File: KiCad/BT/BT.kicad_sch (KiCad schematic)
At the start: 54 parts, among them J1 UJC-HP-3-SMT-TR, J2 2328702-8, J3 Conn_01x05, SW1 PTS840ESDPMSMTRLFS, U1 LDK130PU-R, U2 STBC08PMR, U3 STM6601CQ2BDM6F, U4 BMD-350-A-R, U5 SSM6L61NU, U6 SSM6L61NU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

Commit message: swapped SWDIO/SWCLK, BM pin moved to AN4
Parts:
- R14: value 4M -> 100K
- R15: value 3M -> 75K
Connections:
- net BM: now also U4.45 (P0.28/AIN4); no longer U4.13 (P0.12)
- net BM_EN: now also U4.32 (P0.27); no longer U4.45 (P0.28/AIN4)
- net LED_EN: now also U4.34 (P0.26); no longer U4.32 (P0.27)
- net SWDCLK: now also J3.4 (Pin_4), U4.4 (SWCLK); no longer J3.3 (Pin_3), U4.5 (SWDIO)
- net SWDIO: now also J3.3 (Pin_3), U4.5 (SWDIO); no longer J3.4 (Pin_4), U4.4 (SWCLK)
- net XSHUT1: now also U4.19 (P0.06); no longer U4.12 (P0.13)
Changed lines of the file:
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@@
   (no_connect (at 231.14 64.77))
   (no_connect (at 180.34 49.53))
-  (no_connect (at 231.14 57.15))
+  (no_connect (at 231.14 44.45))
   (no_connect (at 92.71 48.26))
-  (no_connect (at 231.14 74.93))
+  (no_connect (at 180.34 77.47))
   (no_connect (at 250.19 162.56))
   (no_connect (at 231.14 80.01))
   (no_connect (at 64.77 90.17))
   (no_connect (at 180.34 69.85))
-  (no_connect (at 231.14 44.45))
+  (no_connect (at 180.34 74.93))
   (no_connect (at 231.14 46.99))
   (no_connect (at 92.71 53.34))
@@
   (no_connect (at 92.71 55.88))
   (no_connect (at 231.14 59.69))
-  (no_connect (at 180.34 59.69))
+  (no_connect (at 231.14 74.93))
   (no_connect (at 149.86 170.18))
   (no_connect (at 231.14 49.53))
@@
     (stroke (width 0) (type default))
   )
-  (wire (pts (xy 180.34 77.47) (xy 176.53 77.47))
+  (wire (pts (xy 180.34 59.69) (xy 176.53 59.69))
     (stroke (width 0) (type default))
   )
@@
     (stroke (width 0) (type default))
   )
-  (wire (pts (xy 180.34 39.37) (xy 176.53 39.37))
+  (wire (pts (xy 180.34 36.83) (xy 176.53 36.83))
     (stroke (width 0) (type default))
   )
@@
     (stroke (width 0) (type default))
   )
-  (wire (pts (xy 180.34 74.93) (xy 176.53 74.93))
+  (wire (pts (xy 231.14 52.07) (xy 234.95 52.07))
     (stroke (width 0) (type default))
   )
@@
     (stroke (width 0) (type default))
   )
-  (wire (pts (xy 231.14 52.07) (xy 234.95 52.07))
+  (wire (pts (xy 231.14 54.61) (xy 234.95 54.61))
     (stroke (width 0) (type default))
   )
@@
     (stroke (width 0) (type default))
   )
-  (wire (pts (xy 234.95 54.61) (xy 231.14 54.61))
+  (wire (pts (xy 234.95 57.15) (xy 231.14 57.15))
     (stroke (width 0) (type default))
   )
@@
     (stroke (width 0) (type default))
   )
-  (wire (pts (xy 180.34 36.83) (xy 176.53 36.83))
+  (wire (pts (xy 180.34 39.37) (xy 176.53 39.37))
     (stroke (width 0) (type default))
   )
@@
     )
   )
-  (global_label "BM_EN" (shape output) (at 234.95 52.07 0)
+  (global_label "BM_EN" (shape output) (at 234.95 54.61 0)
     (effects (font (size 1.27 1.27)) (justify left))
-    (property "Intersheetrefs" "${INTERSHEET_REFS}" (at 234.95 52.07 0)
+    (property "Intersheetrefs" "${INTERSHEET_REFS}" (at 234.95 54.61 0)
       (effects (font (size 1.27 1.27)) hide)
     )
@@
     )
   )
-  (global_label "SWDIO" (shape output) (at 88.9 78.74 180)
+  (global_label "SWDIO" (shape output) (at 88.9 76.2 180)
     (effects (font (size 1.27 1.27)) (justify right))
-    (property "Intersheetrefs" "${INTERSHEET_REFS}" (at 88.9 78.74 0)
+    (property "Intersheetrefs" "${INTERSHEET_REFS}" (at 88.9 76.2 0)
       (effects (font (size 1.27 1.27)) hide)
     )
@@
     )
   )
-  (global_label "SWDCLK" (shape output) (at 88.9 76.2 180)
+  (global_label "SWDCLK" (shape output) (at 88.9 78.74 180)
     (effects (font (size 1.27 1.27)) (justify right))
-    (property "Intersheetrefs" "${INTERSHEET_REFS}" (at 88.9 76.2 0)
+    (property "Intersheetrefs" "${INTERSHEET_REFS}" (at 88.9 78.74 0)
       (effects (font (size 1.27 1.27)) hide)
     )
@@
     )
   )
-  (global_label "XSHUT1" (shape output) (at 176.53 77.47 180)
+  (global_label "XSHUT1" (shape output) (at 176.53 59.69 180)
     (effects (font (size 1.27 1.27)) (justify right))
-    (property "Intersheetrefs" "${INTERSHEET_REFS}" (at 176.53 77.47 0)
+    (property "Intersheetrefs" "${INTERSHEET_REFS}" (at 176.53 59.69 0)
       (effects (font (size 1.27 1.27)) hide)
     )
@@
     )
   )
-  (global_label "LED_EN" (shape output) (at 234.95 54.61 0)
+  (global_label "LED_EN" (shape output) (at 234.95 57.15 0)
     (effects (font (size 1.27 1.27)) (justify left))
-    (property "Intersheetrefs" "${INTERSHEET_REFS}" (at 234.95 54.61 0)
+    (property "Intersheetrefs" "${INTERSHEET_REFS}" (at 234.95 57.15 0)
       (effects (font (size 1.27 1.27)) hide)
     )
   )
-  (global_label "BM" (shape input) (at 176.53 74.93 180)
-    (effects (font (size 1.27 1.27)) (justify right))
-    (property "Intersheetrefs" "${INTERSHEET_REFS}" (at 176.53 74.93 0)
+  (global_label "BM" (shape input) (at 234.95 52.07 0)
+    (effects (font (size 1.27 1.27)) (justify left))
+    (property "Intersheetrefs" "${INTERSHEET_REFS}" (at 234.95 52.07 0)
       (effects (font (size 1.27 1.27)) hide)
     )
@@
     )
   )
-  (global_label "SWDCLK" (shape input) (at 176.53 39.37 180)
+  (global_label "SWDCLK" (shape input) (at 176.53 36.83 180)
     (effects (font (size 1.27 1.27)) (justify right))
-    (property "Intersheetrefs" "${INTERSHEET_REFS}" (at 176.53 39.37 0)
+    (property "Intersheetrefs" "${INTERSHEET_REFS}" (at 176.53 36.83 0)
       (effects (font (size 1.27 1.27)) hide)
     )
@@
     )
   )
-  (global_label "SWDIO" (shape input) (at 176.53 36.83 180)
+  (global_label "SWDIO" (shape input) (at 176.53 39.37 180)
     (effects (font (size 1.27 1.27)) (justify right))
-    (property "Intersheetrefs" "${INTERSHEET_REFS}" (at 176.53 36.83 0)
+    (property "Intersheetrefs" "${INTERSHEET_REFS}" (at 176.53 39.37 0)
       (effects (font (size 1.27 1.27)) hide)
     )
@@
       (effects (font (size 1.27 1.27)) (justify left))
     )
-    (property "Value" "4M" (at 337.0072 63.373 0)
+    (property "Value" "100K" (at 337.0072 63.373 0)
       (effects (font (size 1.27 1.27)) (justify left))
     )
@@
       (effects (font (size 1.27 1.27)) (justify left))
     )
-    (property "Value" "3M" (at 337.0072 76.073 0)
+    (property "Value" "75K" (at 337.0072 76.073 0)
       (effects (font (size 1.27 1.27)) (justify left))
     )

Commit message: updated sch rev and minor note edit
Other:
- note added: "NOTES: - Vout = (Vin*R15)/(R14+R15) - BM = VBATT @ 4.2V = 1.8V"
- note removed: "NOTES: - Vout = (Vin*R15)/(R14+R15) - BM = 1.8V @ VBATT = 4.2V"
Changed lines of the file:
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@@
   (title_block
     (title "SIDFLC")
-    (rev "V6.0")
+    (rev "V7.0")
     (comment 1 "Designed by Andrew Green")
   )
@@
     (effects (font (size 1.27 1.27)) (justify left bottom))
   )
-  (text "NOTES:\n- Vout = (Vin*R15)/(R14+R15)\n- BM = 1.8V @ VBATT = 4.2V"
+  (text "NOTES:\n- Vout = (Vin*R15)/(R14+R15)\n- BM = VBATT @ 4.2V = 1.8V"
     (at 345.44 64.77 0)
     (effects (font (size 1.27 1.27)) (justify left bottom))

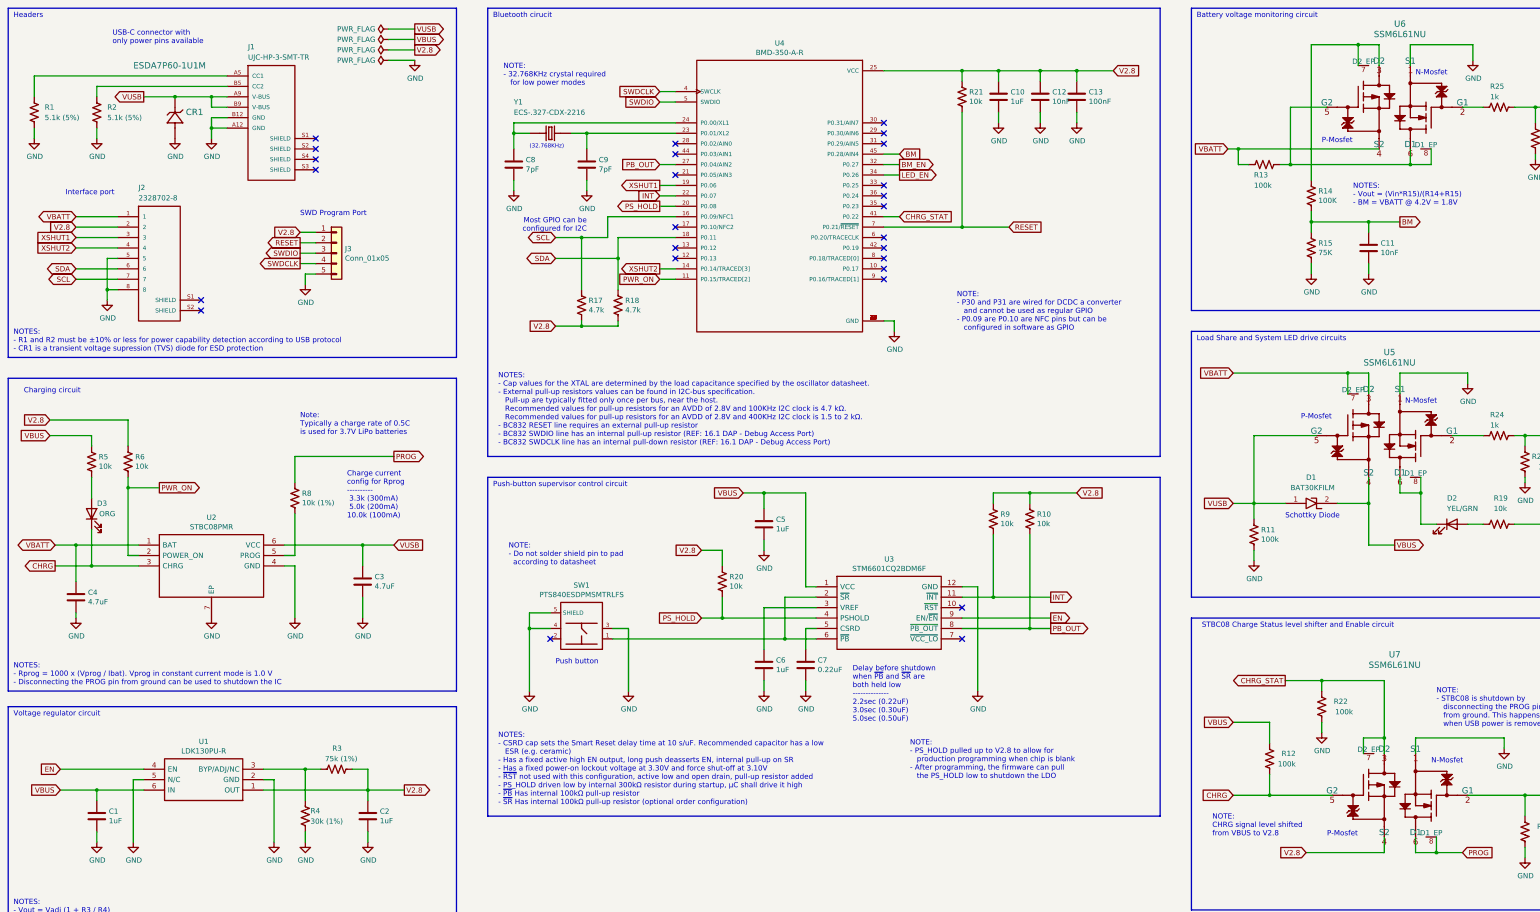
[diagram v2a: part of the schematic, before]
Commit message: updated schematic notes
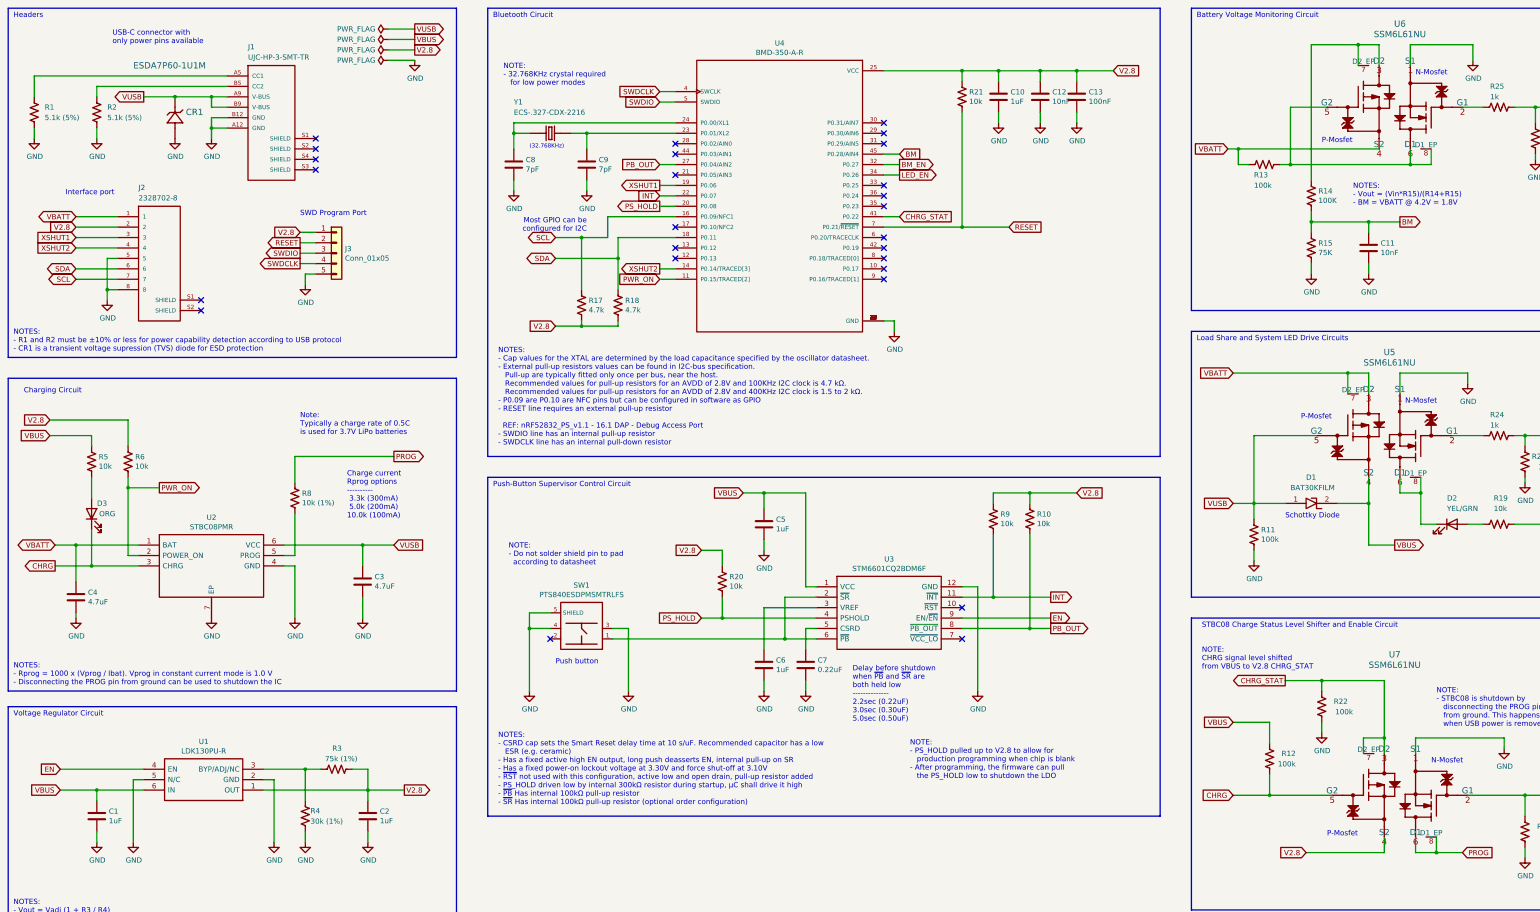
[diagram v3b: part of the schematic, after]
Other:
- note added: "Battery Voltage Monitoring Circuit"
- note added: "Bluetooth Cirucit"
- note added: "Charge current Rprog options ---------- 3.3k (300mA) 5.0k (200mA) 10.0k (100mA)"
- note added: "Charging Circuit"
- note added: "Load Share and System LED Drive Circuits"
- note added: "NOTE: CHRG signal level shifted from VBUS to V2.8 CHRG_STAT"
- note added: "Push-Button Supervisor Control Circuit"
- note added: "STBC08 Charge Status Level Shifter and Enable Circuit"
- note added: "Voltage Regulator Circuit"
- note removed: "Battery voltage monitoring circuit"
- note removed: "Bluetooth cirucit"
- note removed: "Charge current config for Rprog ---------- 3.3k (300mA) 5.0k (200mA) 10.0k (100mA)"
- note removed: "Charging circuit"
- note removed: "Load Share and System LED drive circuits"
- note removed: "NOTE: - P30 and P31 are wired for DCDC a converter and cannot be used as regular GPIO - P0.09 are P0.10 are NFC pins but can be configured in software as GPIO"
- note removed: "NOTE: CHRG signal level shifted from VBUS to V2.8"
- note removed: "Push-button supervisor control circuit"
- note removed: "STBC08 Charge Status level shifter and Enable circuit"
- note removed: "Voltage regulator circuit"
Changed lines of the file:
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@@
     (effects (font (size 1.27 1.27)) (justify left bottom))
   )
-  (text "Charge current\nconfig for Rprog\n----------\n 3.3k (300mA)\n 5.0k (200mA)\n10.0k (100mA)"
+  (text "Charge current\nRprog options\n----------\n 3.3k (300mA)\n 5.0k (200mA)\n10.0k (100mA)"
     (at 100.33 140.97 0)
     (effects (font (size 1.27 1.27)) (justify left bottom))
@@
     (effects (font (size 1.27 1.27)) (justify left bottom))
   )
-  (text "STBC08 Charge Status level shifter and Enable circuit"
+  (text "STBC08 Charge Status Level Shifter and Enable Circuit"
     (at 308.61 167.64 0)
     (effects (font (size 1.27 1.27)) (justify left bottom))
   )
-  (text "NOTES:\n- Cap values for the XTAL are determined by the load capacitance specified by the oscillator datasheet.\n- External pull-up resistors values can be found in I2C-bus specification.\n   Pull-up are typically fitted only once per bus, near the host.\n   Recommended values for pull-up resistors for an AVDD of 2.8V and 100KHz I2C clock is 4.7 kΩ.\n   Recommended values for pull-up resistors for an AVDD of 2.8V and 400KHz I2C clock is 1.5 to 2 kΩ.\n- BC832 RESET line requires an external pull-up resistor\n- BC832 SWDIO line has an internal pull-up resistor (REF: 16.1 DAP - Debug Access Port)\n- BC832 SWDCLK line has an internal pull-down resistor (REF: 16.1 DAP - Debug Access Port)"
+  (text "NOTES:\n- Cap values for the XTAL are determined by the load capacitance specified by the oscillator datasheet.\n- External pull-up resistors values can be found in I2C-bus specification.\n   Pull-up are typically fitted only once per bus, near the host.\n   Recommended values for pull-up resistors for an AVDD of 2.8V and 100KHz I2C clock is 4.7 kΩ.\n   Recommended values for pull-up resistors for an AVDD of 2.8V and 400KHz I2C clock is 1.5 to 2 kΩ.\n- P0.09 are P0.10 are NFC pins but can be configured in software as GPIO\n- RESET line requires an external pull-up resistor\n\n  REF: nRF52832_PS_v1.1 - 16.1 DAP - Debug Access Port\n- SWDIO line has an internal pull-up resistor\n- SWDCLK line has an internal pull-down resistor"
     (at 137.16 123.19 0)
     (effects (font (size 1.27 1.27)) (justify left bottom))
@@
     (effects (font (size 0.9906 0.9906)) (justify left bottom))
   )
-  (text "Voltage regulator circuit" (at 19.05 189.23 0)
+  (text "Voltage Regulator Circuit" (at 19.05 189.23 0)
     (effects (font (size 1.27 1.27)) (justify left bottom))
   )
@@
     (effects (font (size 1.27 1.27)) (justify left bottom))
   )
-  (text "Bluetooth cirucit" (at 135.89 19.05 0)
+  (text "Bluetooth Cirucit" (at 135.89 19.05 0)
     (effects (font (size 1.27 1.27)) (justify left bottom))
   )
@@
     (effects (font (size 1.27 1.27)) (justify left bottom))
   )
-  (text "Load Share and System LED drive circuits" (at 307.34 97.79 0)
+  (text "Load Share and System LED Drive Circuits" (at 307.34 97.79 0)
     (effects (font (size 1.27 1.27)) (justify left bottom))
   )
-  (text "Battery voltage monitoring circuit" (at 307.34 19.05 0)
+  (text "Battery Voltage Monitoring Circuit" (at 307.34 19.05 0)
     (effects (font (size 1.27 1.27)) (justify left bottom))
   )
-  (text "NOTE:\nCHRG signal level shifted\nfrom VBUS to V2.8" (at 311.15 218.44 0)
+  (text "NOTE:\nCHRG signal level shifted\nfrom VBUS to V2.8 CHRG_STAT"
+    (at 308.61 177.8 0)
     (effects (font (size 1.27 1.27)) (justify left bottom))
   )
@@
     (effects (font (size 1.27 1.27)) (justify left bottom))
   )
-  (text "Push-button supervisor control circuit" (at 135.89 133.35 0)
+  (text "Push-Button Supervisor Control Circuit" (at 135.89 133.35 0)
     (effects (font (size 1.27 1.27)) (justify left bottom))
   )
@@
     (effects (font (size 1.27 1.27)) (justify left bottom))
   )
-  (text "Charging circuit" (at 21.59 110.49 0)
+  (text "Charging Circuit" (at 21.59 110.49 0)
     (effects (font (size 1.27 1.27)) (justify left bottom))
   )
@@
     (effects (font (size 1.27 1.27)) (justify left bottom))
   )
-  (text "NOTE:\n- P30 and P31 are wired for DCDC a converter\n   and cannot be used as regular GPIO\n- P0.09 are P0.10 are NFC pins but can be\n   configured in software as GPIO"
-    (at 248.92 95.25 0)
-    (effects (font (size 1.27 1.27)) (justify left bottom))
-  )
